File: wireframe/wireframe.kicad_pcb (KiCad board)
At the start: 2 copper layers, 37 parts, among them U1 ESP32-S2-DevKitC-1

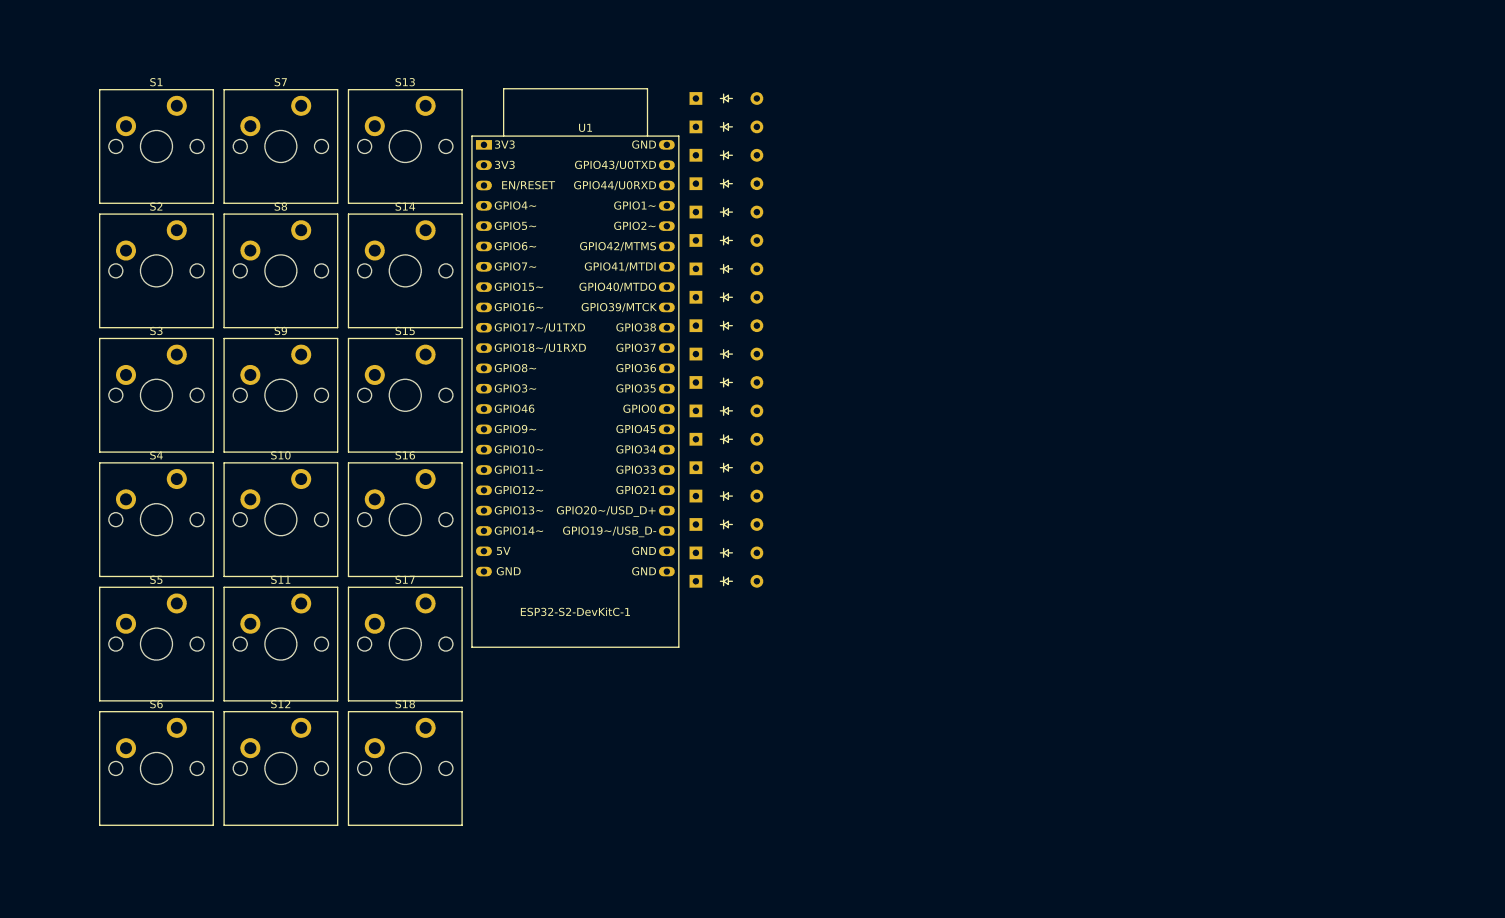
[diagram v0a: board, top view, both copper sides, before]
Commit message: Finalize layout and fully traced to ESP32
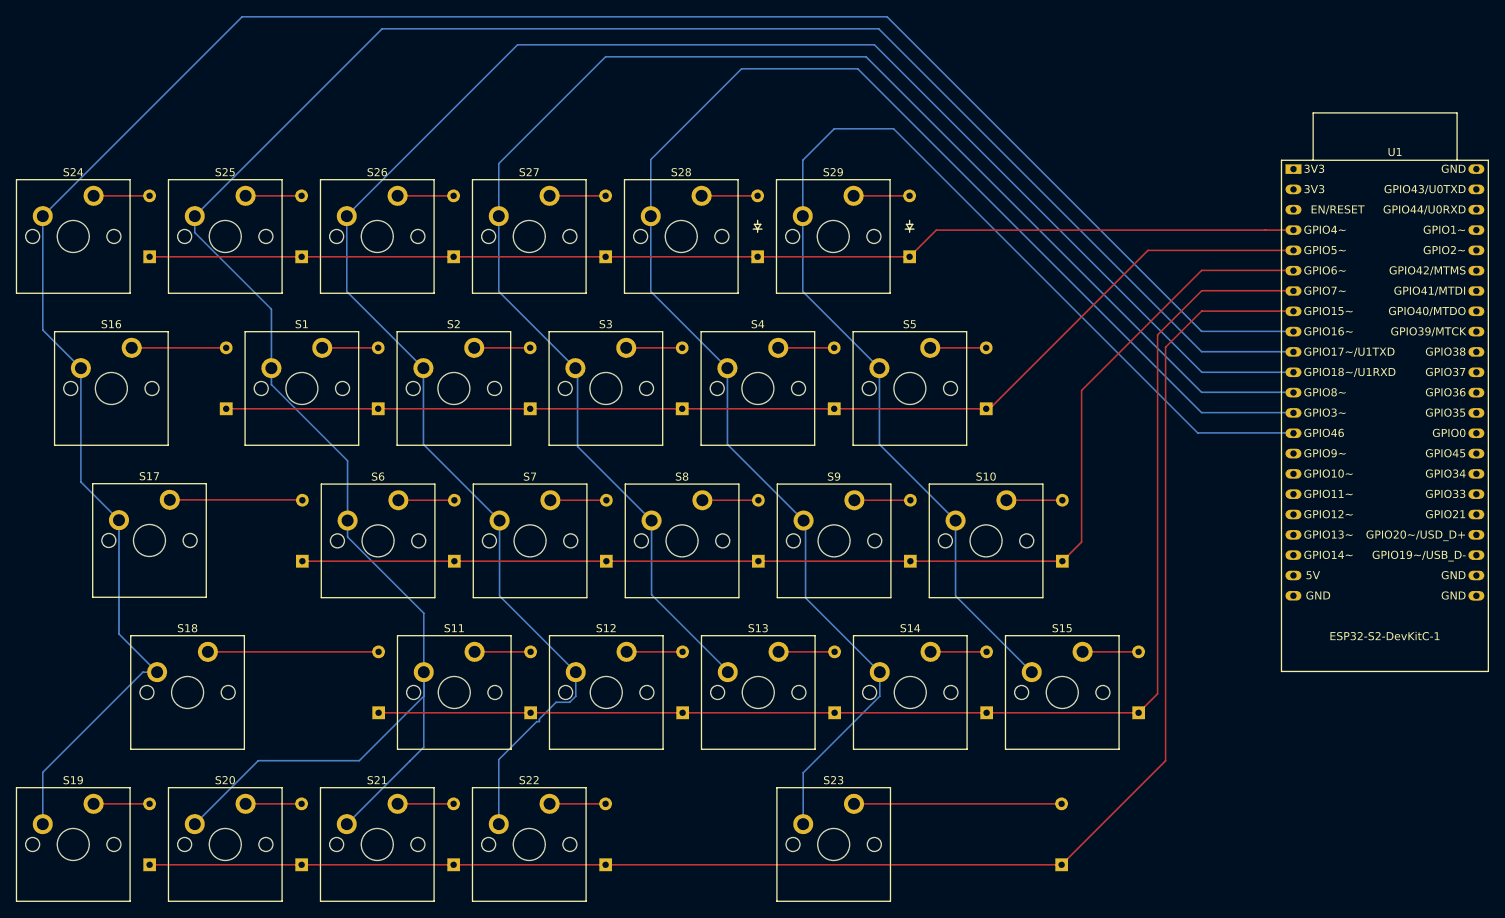
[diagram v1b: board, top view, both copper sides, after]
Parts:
- added D19: Diode, ScottoKeebs_Components:Diode_DO-35, B.Cu at (58.5, 127.5)
- added D20: Diode, ScottoKeebs_Components:Diode_DO-35, B.Cu at (77.5, 127.5)
- added D21: Diode, ScottoKeebs_Components:Diode_DO-35, B.Cu at (96.5, 127.5)
- added D22: Diode, ScottoKeebs_Components:Diode_DO-35, B.Cu at (115.5, 127.5)
- added D23: Diode, ScottoKeebs_Components:Diode_DO-35, B.Cu at (172.5, 127.5)
- added D24: Diode, ScottoKeebs_Components:Diode_DO-35, B.Cu at (58.5, 51.5)
- added D25: Diode, ScottoKeebs_Components:Diode_DO-35, B.Cu at (77.5, 51.5)
- added D26: Diode, ScottoKeebs_Components:Diode_DO-35, B.Cu at (96.5, 51.5)
- added D27: Diode, ScottoKeebs_Components:Diode_DO-35, B.Cu at (115.5, 51.5)
- added D28: Diode, ScottoKeebs_Components:Diode_DO-35, F.Cu at (134.5, 51.5)
- added D29: Diode, ScottoKeebs_Components:Diode_DO-35, F.Cu at (153.5, 51.5)
- added S19: Keyswitch, ScottoKeebs_MX:MX_PCB_1.00u, F.Cu at (49.0, 125.0)
- added S20: Keyswitch, ScottoKeebs_MX:MX_PCB_1.00u, F.Cu at (68.0, 125.0)
- added S21: Keyswitch, ScottoKeebs_MX:MX_PCB_1.00u, F.Cu at (87.0, 125.0)
- added S22: Keyswitch, ScottoKeebs_MX:MX_PCB_1.00u, F.Cu at (106.0, 125.0)
- added S23: Keyswitch, ScottoKeebs_MX:MX_PCB_3.00u, F.Cu at (144.1, 125.0)
- added S24: Keyswitch, ScottoKeebs_MX:MX_PCB_1.00u, F.Cu at (49.0, 49.0)
- added S25: Keyswitch, ScottoKeebs_MX:MX_PCB_1.00u, F.Cu at (68.0, 49.0)
- added S26: Keyswitch, ScottoKeebs_MX:MX_PCB_1.00u, F.Cu at (87.0, 49.0)
- added S27: Keyswitch, ScottoKeebs_MX:MX_PCB_1.00u, F.Cu at (106.0, 49.0)
- added S28: Keyswitch, ScottoKeebs_MX:MX_PCB_1.00u, F.Cu at (125.0, 49.0)
- added S29: Keyswitch, ScottoKeebs_MX:MX_PCB_1.00u, F.Cu at (144.0, 49.0)
- D1, D10, D11, D12, D13, D14, D15, D16, D17, D18, D2, D3, D4, D5, D6, D7, D8, D9: moved to B.Cu
- moved U1 101.2 mm to (201.5, 40.6)
- moved S5 99.4 mm to (153.6, 68.0)
- moved S15 90.1 mm to (172.6, 106.0)
- moved S10 88.2 mm to (163.1, 87.0)
- moved S14 82.2 mm to (153.6, 106.0)
- moved S13 81.3 mm to (134.6, 106.0)
- moved S4 76.9 mm to (134.6, 68.0)
- moved S9 71.5 mm to (144.1, 87.0)
- moved D15 61.6 mm to (182.2, 108.5), turned to 90 degrees
- moved D16 60.5 mm to (68.1, 70.5), turned to 90 degrees
- moved S8 60.4 mm to (125.1, 87.0)
- moved S7 58.3 mm to (106.1, 87.0)
- moved S3 56.2 mm to (115.6, 68.0)
- moved D1 55.5 mm to (87.1, 70.5), turned to 90 degrees
- moved D10 52.6 mm to (172.6, 89.6), turned to 90 degrees
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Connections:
- S1 pad 1: Net-(S1-Pad1) -> Net-(U1-GPIO17/ADC2_CH6/U1TXD)
- S10 pad 1: Net-(S10-Pad1) -> Net-(U1-GPIO46)
- S11 pad 1: Net-(S1-Pad1) -> Net-(U1-GPIO17/ADC2_CH6/U1TXD)
- S12 pad 1: Net-(S12-Pad1) -> Net-(U1-GPIO18/ADC2_CH7/U1RXD)
- S13 pad 1: Net-(S13-Pad1) -> Net-(U1-GPIO8/ADC1_CH7)
- S14 pad 1: Net-(S14-Pad1) -> Net-(U1-GPIO3/ADC1_CH2)
- S15 pad 1: Net-(S10-Pad1) -> Net-(U1-GPIO46)
- S16 pad 1: Net-(S16-Pad1) -> Net-(U1-GPIO16/ADC2_CH5/32K_N)
- S17 pad 1: Net-(S16-Pad1) -> Net-(U1-GPIO16/ADC2_CH5/32K_N)
- S18 pad 1: Net-(S16-Pad1) -> Net-(U1-GPIO16/ADC2_CH5/32K_N)
- S2 pad 1: Net-(S12-Pad1) -> Net-(U1-GPIO18/ADC2_CH7/U1RXD)
- S3 pad 1: Net-(S13-Pad1) -> Net-(U1-GPIO8/ADC1_CH7)
- S4 pad 1: Net-(S14-Pad1) -> Net-(U1-GPIO3/ADC1_CH2)
- S5 pad 1: Net-(S10-Pad1) -> Net-(U1-GPIO46)
- S6 pad 1: Net-(S1-Pad1) -> Net-(U1-GPIO17/ADC2_CH6/U1TXD)
- S7 pad 1: Net-(S12-Pad1) -> Net-(U1-GPIO18/ADC2_CH7/U1RXD)
- S8 pad 1: Net-(S13-Pad1) -> Net-(U1-GPIO8/ADC1_CH7)
- S9 pad 1: Net-(S14-Pad1) -> Net-(U1-GPIO3/ADC1_CH2)
- U1 pad 10: unconnected-(U1-GPIO17/ADC2_CH6/U1TXD-Pad10) -> Net-(U1-GPIO17/ADC2_CH6/U1TXD)
- U1 pad 11: unconnected-(U1-GPIO18/ADC2_CH7/U1RXD-Pad11) -> Net-(U1-GPIO18/ADC2_CH7/U1RXD)
- U1 pad 12: unconnected-(U1-GPIO8/ADC1_CH7-Pad12) -> Net-(U1-GPIO8/ADC1_CH7)
- U1 pad 13: unconnected-(U1-GPIO3/ADC1_CH2-Pad13) -> Net-(U1-GPIO3/ADC1_CH2)
- U1 pad 14: unconnected-(U1-GPIO46-Pad14) -> Net-(U1-GPIO46)
- U1 pad 4: unconnected-(U1-GPIO4/ADC1_CH3-Pad4) -> Net-(D24-K)
- U1 pad 5: unconnected-(U1-GPIO5/ADC1_CH4-Pad5) -> Net-(D1-K)
- U1 pad 6: unconnected-(U1-GPIO6/ADC1_CH5-Pad6) -> Net-(D10-K)
- U1 pad 7: unconnected-(U1-GPIO7/ADC1_CH6-Pad7) -> Net-(D11-K)
- U1 pad 8: unconnected-(U1-GPIO15/ADC2_CH4/32K_P-Pad8) -> Net-(D19-K)
- U1 pad 9: unconnected-(U1-GPIO16/ADC2_CH5/32K_N-Pad9) -> Net-(U1-GPIO16/ADC2_CH5/32K_N)
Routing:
- net Net-(U1-GPIO17/ADC2_CH6/U1TXD): track 0.00 -> 294.0 mm
- net Net-(U1-GPIO16/ADC2_CH5/32K_N): track 0.00 -> 271.8 mm
- net Net-(U1-GPIO18/ADC2_CH7/U1RXD): track 0.00 -> 237.3 mm
- net Net-(U1-GPIO3/ADC1_CH2): track 0.00 -> 203.0 mm
- net Net-(D19-K): track 0.00 -> 202.0 mm
- net Net-(U1-GPIO8/ADC1_CH7): track 0.00 -> 197.7 mm
- net Net-(D11-K): track 0.00 -> 162.5 mm
- net Net-(U1-GPIO46): track 0.00 -> 154.6 mm
- net Net-(D10-K): track 0.00 -> 150.0 mm
- net Net-(D24-K): track 0.00 -> 144.4 mm
- net Net-(D1-K): track 0.00 -> 141.6 mm
- net Net-(D23-A): track 0.00 -> 25.9 mm
- net Net-(D18-A): track 0.00 -> 21.3 mm
- net Net-(D17-A): track 0.00 -> 16.6 mm
- net Net-(D16-A): track 0.00 -> 11.8 mm
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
